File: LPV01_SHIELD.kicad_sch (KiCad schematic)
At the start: 98 parts, among them J1 Screw_Terminal_01x02, J10 SPI_header, J11 Power_socket, J12 USB1035-GF-P-0-B-B, J13 USB1035-GF-P-0-B-B, J14 USB1035-GF-P-0-B-B, J15 Screw_Terminal_01x03, J16 Screw_Terminal_01x03, J17 Wiegand, J18 A-USBSA, J19 Screw_Terminal_01x02, J2 Screw_Terminal_01x02, J20 Screw_Terminal_01x02, J21 Screw_Terminal_01x02, J22 Screw_Terminal_01x02, J23 GND, J3 Screw_Terminal_01x02, J4 Screw_Terminal_01x02, J5 Screw_Terminal_01x02, J6 Screw_Terminal_01x02, J7 Screw_Terminal_01x02, J8 Screw_Terminal_01x02, J9 GPIO_header, Q1 BC817, Q2 BC817, Q3 BC817, Q4 BC817, Q5 BC817, Q6 BC817, Q7 BC817, Q8 BC817, SW1 SW_SPST, SW2 SW_SPST, SW3 SW_SPST, SW4 SW_SPST, SW5 SW_SPST, SW6 SW_SPST, SW7 SW_SPST, SW8 SW_SPST, U1 TLP175A, U12 USB2517I-JZX, U13 FT2232HQ, U16 M24C02-FMN, U2 TLP175A, U3 TLP175A, U4 TLP175A, U5 TLP175A, U6 TLP175A, U7 TLP175A, U8 TLP175A

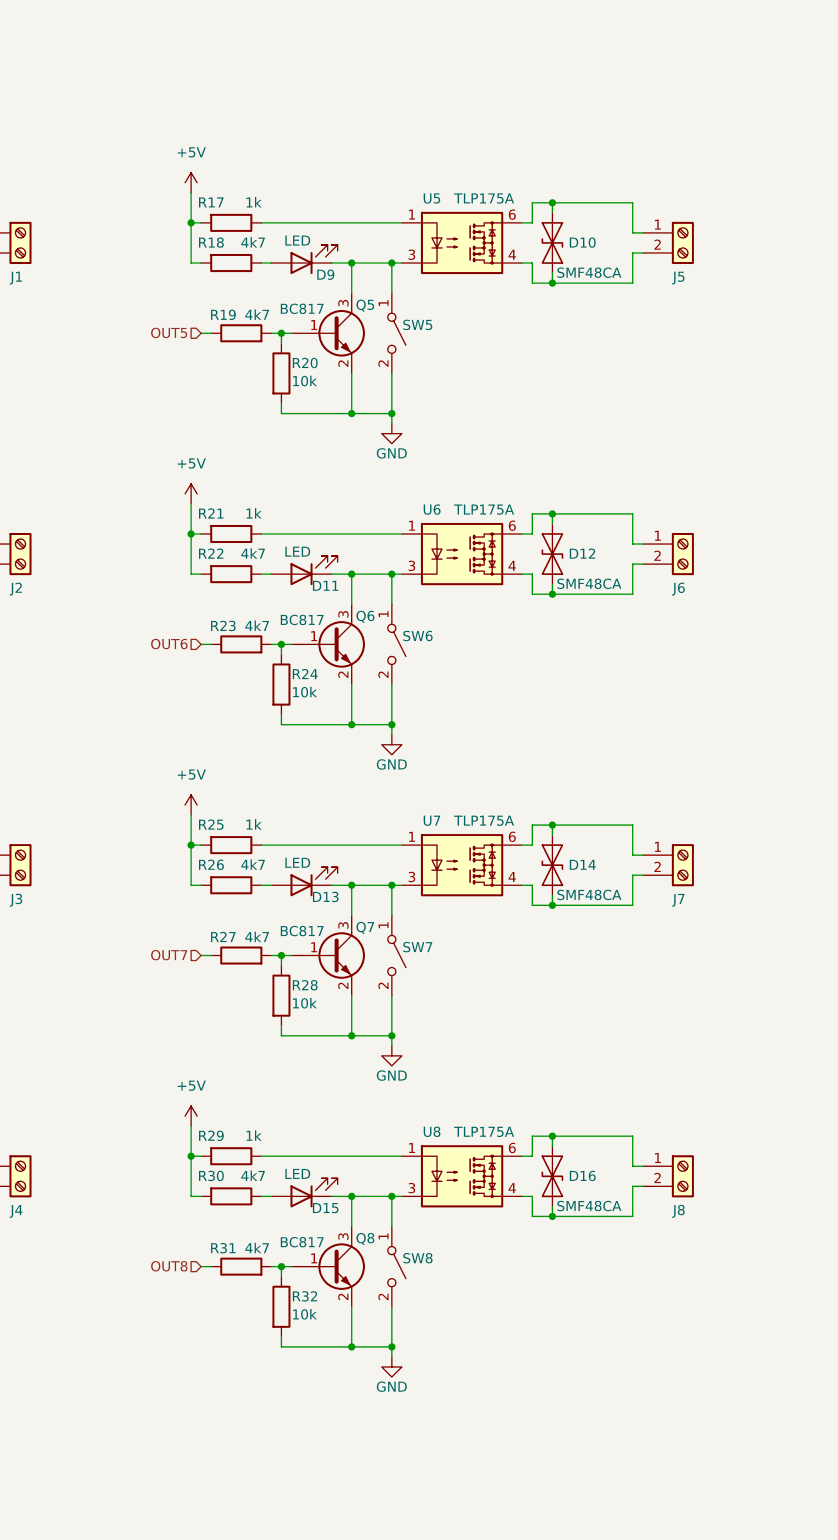
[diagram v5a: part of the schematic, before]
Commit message: Changes in schematic to fit DC/DC converter
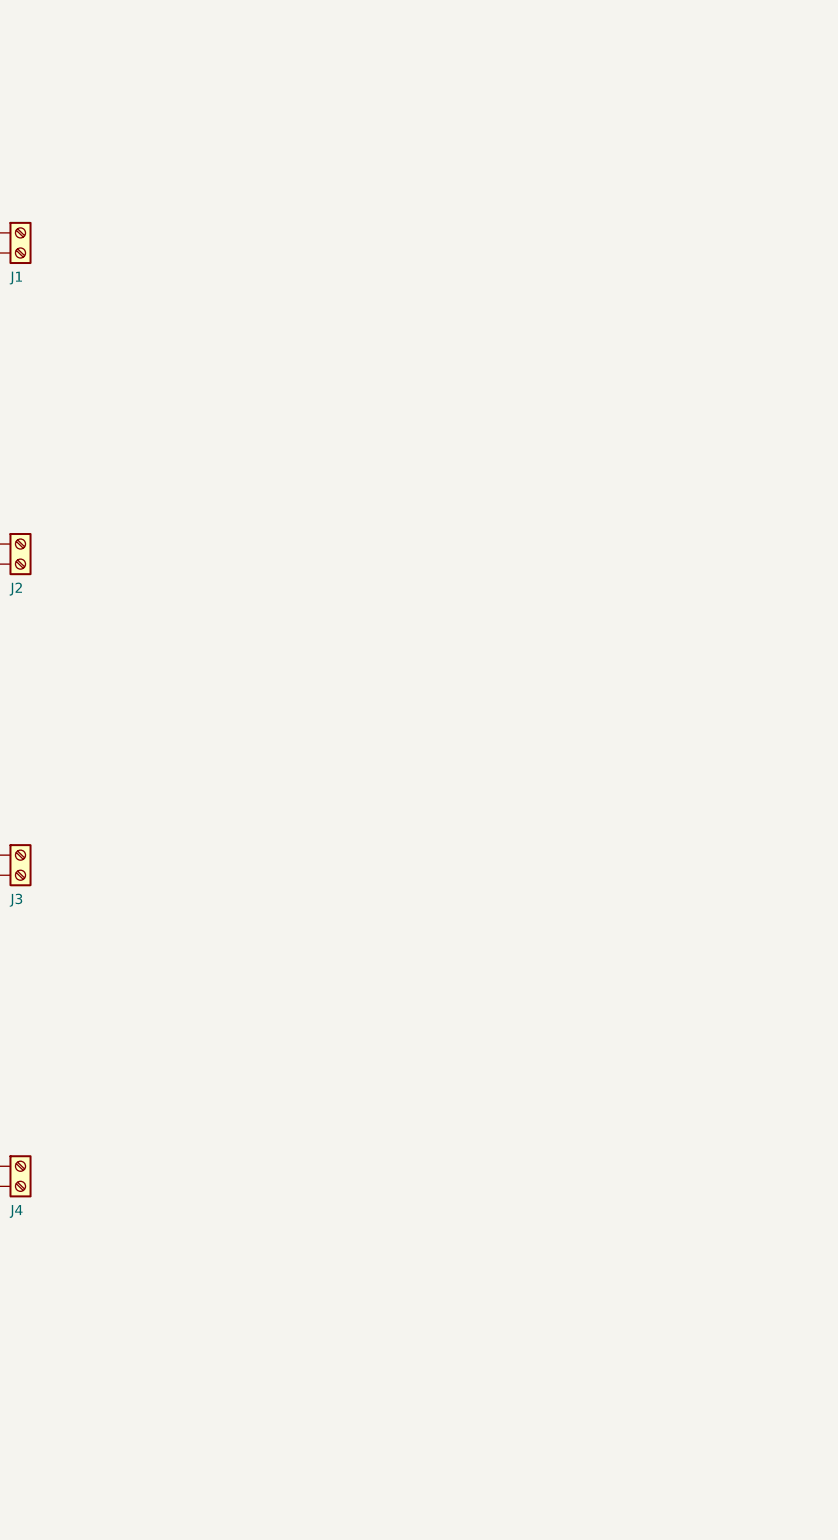
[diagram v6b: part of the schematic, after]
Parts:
- removed D10, D12, D14, D16: SMF48CA, Diode_SMD:D_SMA, symbol Diode:SD36_SOD323
- removed D11, D13, D15, D9: LED, LED_SMD:LED_0603_1608Metric, symbol Device:LED
- removed J5, J6, J7, J8: Screw_Terminal_01x02, TerminalBlock_Phoenix:TerminalBlock_Phoenix_MKDS-1,5-2_1x02_P5.00mm_Horizontal, symbol Connector:Screw_Terminal_01x02
- removed Q5, Q6, Q7, Q8: BC817, Package_TO_SOT_SMD:SOT-23, symbol Transistor_BJT:BC817
- removed R17, R21, R25, R29: 1k, Resistor_SMD:R_0603_1608Metric, symbol Device:R
- removed R18, R19, R22, R23, R26, R27, R30, R31: 4k7, Resistor_SMD:R_0603_1608Metric, symbol Device:R
- removed R20, R24, R28, R32: 10k, Resistor_SMD:R_0603_1608Metric, symbol Device:R
- removed SW5, SW6, SW7, SW8: SW_SPST, Button_Switch_SMD:SW_SPST_CK_RS282G05A3, symbol Switch:SW_SPST
- removed U5, U6, U7, U8: TLP175A, Package_SO:MFSOP6-4_4.4x3.6mm_P1.27mm, symbol Relay_SolidState:TLP175A

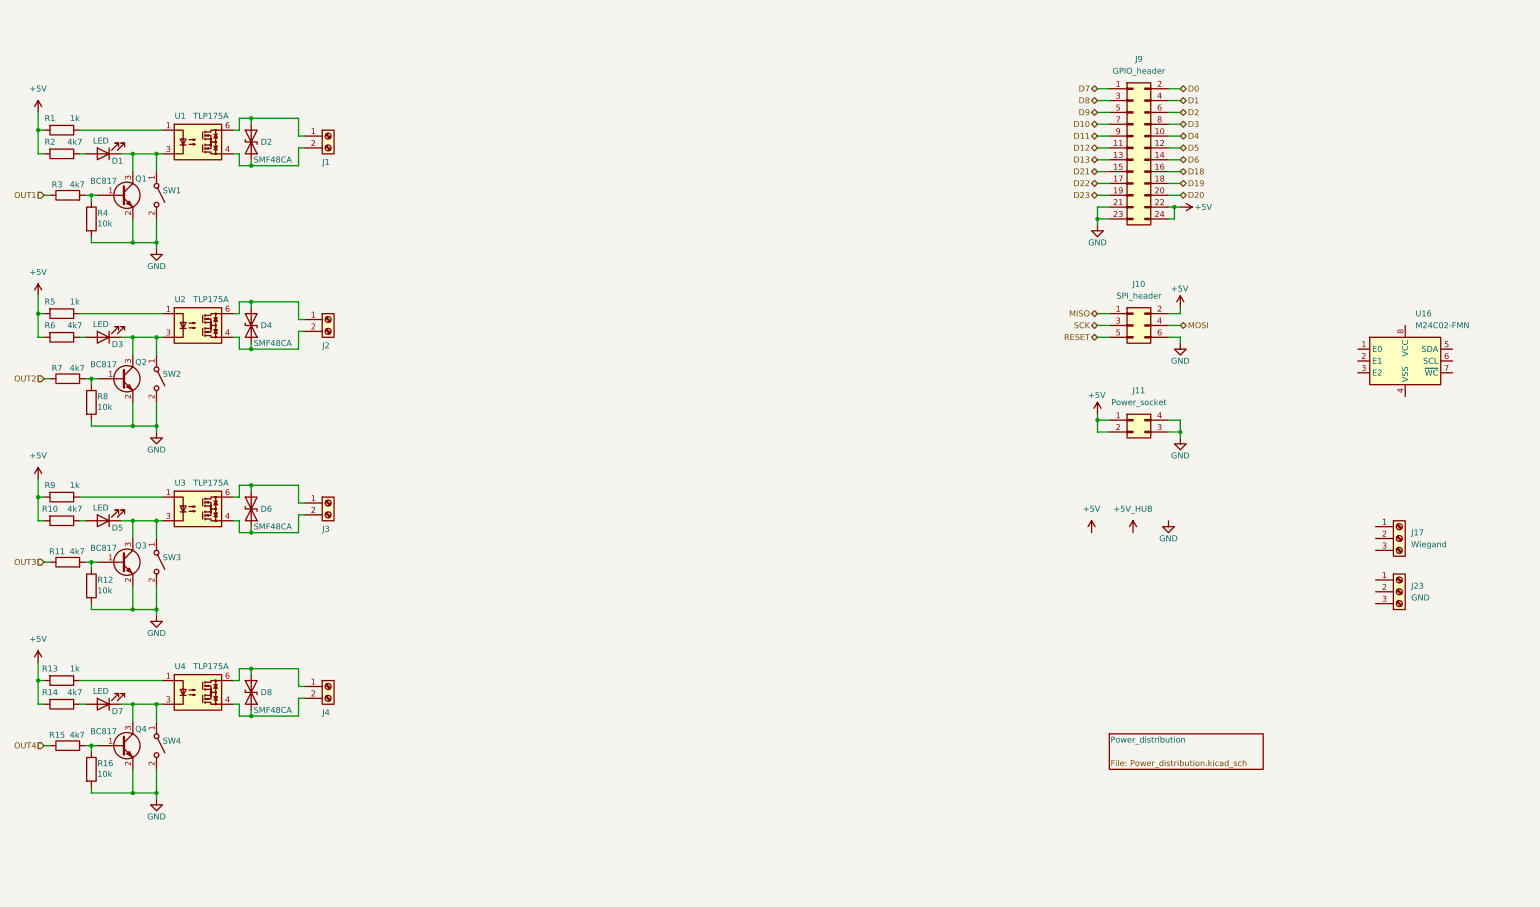
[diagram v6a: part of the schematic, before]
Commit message: Added 2 schematic sheets
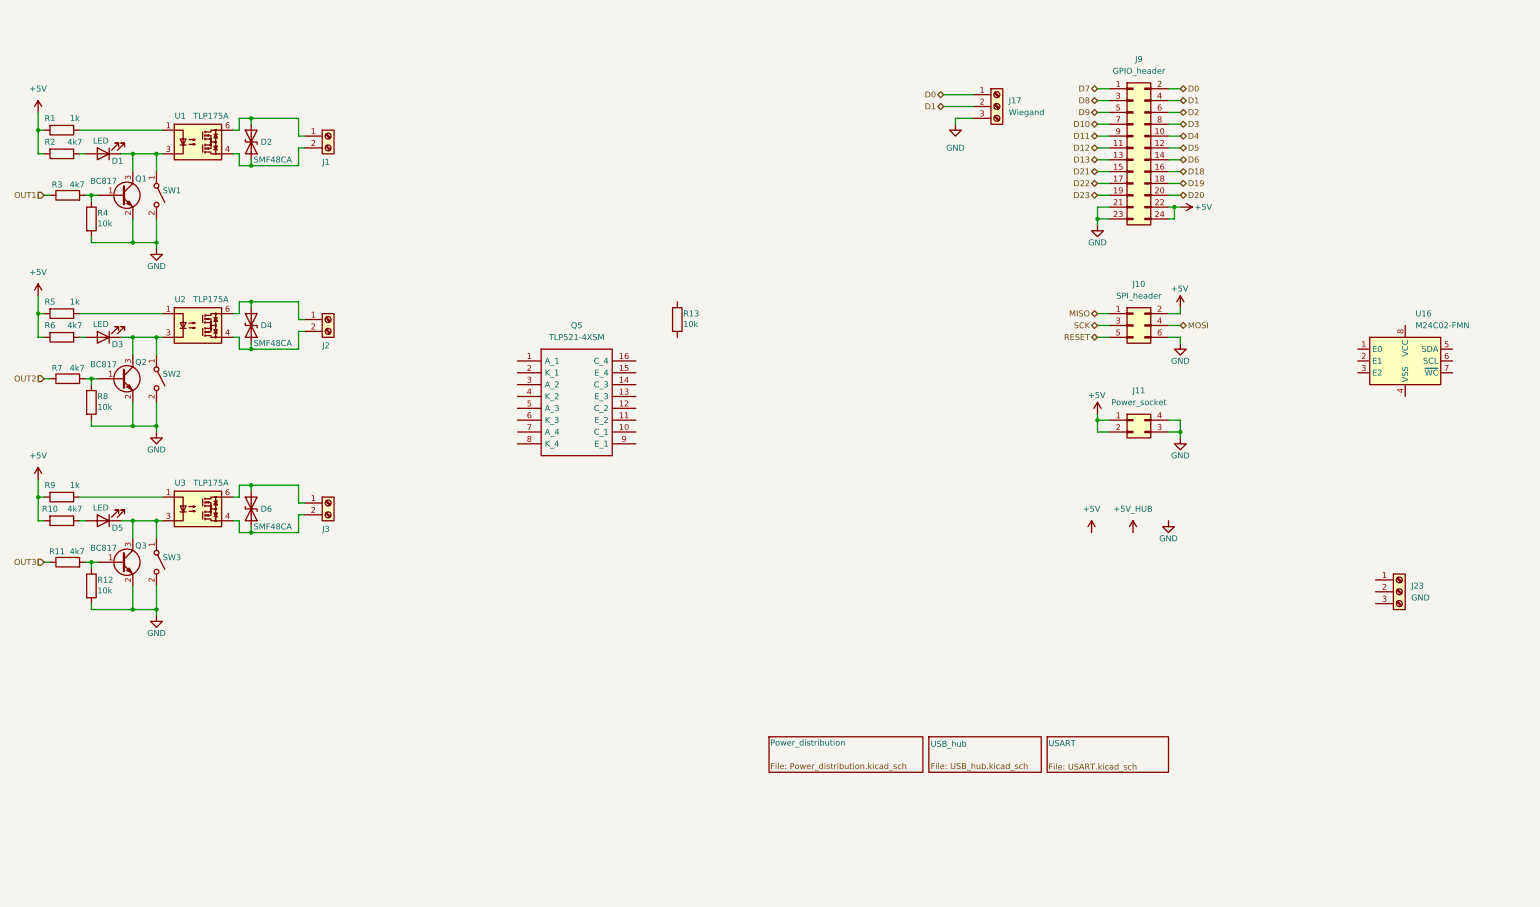
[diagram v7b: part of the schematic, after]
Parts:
- removed D7: LED, LED_SMD:LED_0603_1608Metric, symbol Device:LED
- removed D8: SMF48CA, Diode_SMD:D_SMA, symbol Diode:SD36_SOD323
- removed J4: Screw_Terminal_01x02, TerminalBlock_Phoenix:TerminalBlock_Phoenix_MKDS-1,5-2_1x02_P5.00mm_Horizontal, symbol Connector:Screw_Terminal_01x02
- removed Q4: BC817, Package_TO_SOT_SMD:SOT-23, symbol Transistor_BJT:BC817
- removed R14, R15: 4k7, Resistor_SMD:R_0603_1608Metric, symbol Device:R
- removed R16: 10k, Resistor_SMD:R_0603_1608Metric, symbol Device:R
- removed SW4: SW_SPST, Button_Switch_SMD:SW_SPST_CK_RS282G05A3, symbol Switch:SW_SPST
- removed U4: TLP175A, Package_SO:MFSOP6-4_4.4x3.6mm_P1.27mm, symbol Relay_SolidState:TLP175A
- added Q5: TLP521-4XSM, SamacSys_Parts:TLP5214XSM, symbol SamacSys_Parts:TLP521-4XSM
- J17: footprint TerminalBlock_Phoenix:TerminalBlock_Phoenix_MKDS-1,5-3_1x03_P5.00mm_Horizontal -> TerminalBlock_Phoenix:TerminalBlock_Phoenix_PT-1,5-3-3.5-H_1x03_P3.50mm_Horizontal
- J18: footprint A-USBSA -> SamacSys_Parts:A-USBSA
- R13: value 1k -> 10k
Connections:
- net +5V: no longer R13.2
- net D0: now also J17.1 (Pin_1)
- net D1: now also J17.2 (Pin_2)
- net GND: now also J17.3 (Pin_3)
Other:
- added sheet USART (USART.kicad_sch)
- added sheet USB_hub (USB_hub.kicad_sch)
- moved on the sheet: J17

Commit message: Added inputs and outputs to the schematic
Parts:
- removed J12, J13, J14: USB1035-GF-P-0-B-B, SamacSys_Parts:USB1035GFP0BB, symbol SamacSys_Parts:USB1035-GF-P-0-B-B
- removed J15, J16: Screw_Terminal_01x03, TerminalBlock_Phoenix:TerminalBlock_Phoenix_MKDS-1,5-3_1x03_P5.00mm_Horizontal, symbol Connector:Screw_Terminal_01x03
- removed J18: A-USBSA, SamacSys_Parts:A-USBSA, symbol SamacSys_Parts:A-USBSA
- removed J19, J20, J21, J22: Screw_Terminal_01x02, TerminalBlock_Phoenix:TerminalBlock_Phoenix_MKDS-1,5-2_1x02_P5.00mm_Horizontal, symbol Connector:Screw_Terminal_01x02
- removed J23: GND, TerminalBlock_Phoenix:TerminalBlock_Phoenix_MKDS-1,5-3_1x03_P5.00mm_Horizontal, symbol Connector:Screw_Terminal_01x03
- removed U12: USB2517I-JZX, Package_DFN_QFN:QFN-64-1EP_9x9mm_P0.5mm_EP5.45x5.45mm_ThermalVias, symbol SamacSys_Parts:USB2517I-JZX
- removed U13: FT2232HQ, Package_DFN_QFN:QFN-64-1EP_9x9mm_P0.5mm_EP4.35x4.35mm, symbol Interface_USB:FT2232HQ
- removed U16: M24C02-FMN, Package_SO:SOIC-8_3.9x4.9mm_P1.27mm, symbol Memory_EEPROM:M24C02-FMN
- added D10, D11, D12, D13, D14, D15, D7, D8: LED, symbol Device:LED
- added D16, D19, D21, D23, D25, D27, D30, D31: D, symbol Device:D
- added D17, D18, D20, D22, D24, D26, D28, D29: LED, LED_SMD:LED_0603_1608Metric, symbol Device:LED
- added J15, J22: Inputs, TerminalBlock_Phoenix:TerminalBlock_Phoenix_PT-1,5-8-3.5-H_1x08_P3.50mm_Horizontal, symbol Connector:Screw_Terminal_01x08
- added J16, J23: Screw_Terminal_01x02, TerminalBlock_Phoenix:TerminalBlock_Phoenix_PT-1,5-2-3.5-H_1x02_P3.50mm_Horizontal, symbol Connector:Screw_Terminal_01x02
- added J24: Conn_01x02_Pin, symbol Connector:Conn_01x02_Pin
- added Q10, Q11, Q12, Q13, Q14, Q15, Q7, Q9: BC817, Package_TO_SOT_SMD:SOT-23, symbol Transistor_BJT:BC817
- added Q4, Q6, Q8: TLP521-4XSM, SamacSys_Parts:TLP5214XSM, symbol SamacSys_Parts:TLP521-4XSM
- added R14, R29, R30, R31, R32, R33, R34, R35: 2k2, Resistor_SMD:R_0603_1608Metric, symbol Device:R
- added R15, R16, R28, R36, R38, R39, R40, R41, R42, R43, R44, R45, R46, R47: 10k, Resistor_SMD:R_0603_1608Metric, symbol Device:R
- added R37: 10k ->, Resistor_SMD:R_0603_1608Metric, symbol Device:R
- added R48, R49, R50, R51, R52, R53, R54, R55, R56, R57, R58, R59, R60, R61, R62, R63: 1k, Resistor_SMD:R_0603_1608Metric, symbol Device:R
- added SW10, SW11, SW4, SW5, SW6, SW7, SW8, SW9: SW_SPST, Button_Switch_SMD:SW_SPST_CK_RS282G05A3, symbol Switch:SW_SPST
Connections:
- net +5V: now also R13.1, Q6.10 (C_1), Q6.12 (C_2), Q6.14 (C_3), Q6.16 (C_4), Q8.10 (C_1), Q8.12 (C_2), Q8.14 (C_3), Q8.16 (C_4), R15.1, R16.1, R28.1, R44.1, R45.1, R46.1, R47.1, SW10.1 (A), SW11.1 (A), SW4.1 (A), SW5.1 (A), SW6.1 (A), SW7.1 (A), SW8.1 (A), SW9.1 (A)
- net D10: now also R49.2
- net D11: now also R50.2
- net D12: now also R51.2
- net D18: now also R53.2
- net D19: now also R54.2
- net D2: now also Q5.16 (C_4), R13.2
- net D21: now also R52.2
- net D22: now also R55.2
- net D23: now also R56.2
- net D3: now also Q5.14 (C_3), R15.2
- net D4: now also Q5.12 (C_2), R16.2
- net D5: now also Q5.10 (C_1), R28.2
- net D6: now also Q4.16 (C_4), R44.2
- net D7: now also Q4.14 (C_3), R45.2
- net D8: now also Q4.12 (C_2), R46.2
- net D9: now also Q4.10 (C_1), R47.2
- net GND: now also Q5.11 (E_2), Q5.13 (E_3), Q5.15 (E_4), Q5.9 (E_1), J16.1 (Pin_1), J16.2 (Pin_2), J23.2 (Pin_2), Q10.2 (E), Q11.2 (E), Q12.2 (E), Q13.2 (E), Q14.2 (E), Q15.2 (E), Q4.11 (E_2), Q4.13 (E_3), Q4.15 (E_4), Q4.9 (E_1), Q6.2 (K_1), Q6.4 (K_2), Q6.6 (K_3), Q6.8 (K_4), Q7.2 (E), Q8.2 (K_1), Q8.4 (K_2), Q8.6 (K_3), Q8.8 (K_4), Q9.2 (E)
- net MISO: now also R3.1
- net MOSI: now also R11.1
- net OUT1: now also D16.2 (A), J22.1 (Pin_1), Q7.3 (C); no longer R3.1
- net OUT2: now also D19.2 (A), J22.2 (Pin_2), Q9.3 (C); no longer R7.1
- net OUT3: now also D21.2 (A), J22.3 (Pin_3), Q10.3 (C); no longer R11.1
- net SCK: now also R7.1
- net at Q5.1 (A_1): now also D7.1 (K)
- net at Q5.2 (K_1): now also J15.8 (Pin_8), R37.2
- net at Q5.3 (A_2): now also D10.1 (K)
- net at Q5.4 (K_2): now also J15.7 (Pin_7), R36.2
- net at Q5.5 (A_3): now also D11.1 (K)
- net at Q5.6 (K_3): now also J15.6 (Pin_6), R38.2
- net at Q5.7 (A_4): now also D8.1 (K)
- net at Q5.8 (K_4): now also J15.5 (Pin_5), R39.2
- new net: Q12.1 (B), R60.2
- new net: D29.1 (K), R63.1
- new net: Q10.1 (B), R58.2
- new net: Q7.1 (B), R48.2
- new net: D12.1 (K), Q4.1 (A_1)
- new net: D12.2 (A), R32.1
- new net: D10.2 (A), R29.1
- new net: J15.4 (Pin_4), Q4.2 (K_1), R40.2
- new net: D13.1 (K), Q4.3 (A_2)
- new net: J15.3 (Pin_3), Q4.4 (K_2), R41.2
- new net: D14.1 (K), Q4.5 (A_3)
- new net: J15.2 (Pin_2), Q4.6 (K_3), R42.2
- new net: D15.1 (K), Q4.7 (A_4)
- new net: J15.1 (Pin_1), Q4.8 (K_4), R43.2
- new net: D15.2 (A), R35.1
- new net: D17.1 (K), R48.1
- new net: D11.2 (A), R30.1
- new net: Q8.5 (A_3), R55.1
- new net: Q8.1 (A_1), R53.1
- new net: Q8.3 (A_2), R54.1
- new net: Q8.7 (A_4), R56.1
- new net: D22.1 (K), R59.1
- new net: Q11.1 (B), R59.2
- new net: Q14.1 (B), R62.2
- new net: D13.2 (A), R33.1
- new net: D18.1 (K), R57.1
- new net: D20.1 (K), R58.1
- new net: D7.2 (A), R14.1
- new net: D14.2 (A), R34.1
- new net: Q13.1 (B), R61.2
- new net: D8.2 (A), R31.1
- new net: Q6.1 (A_1), R49.1
- new net: Q6.3 (A_2), R50.1
- new net: Q6.5 (A_3), R51.1
- new net: Q6.7 (A_4), R52.1
- new net: Q9.1 (B), R57.2
- new net: D26.1 (K), R61.1
- new net: Q15.1 (B), R63.2
- new net: D24.1 (K), R60.1
- new net: D28.1 (K), R62.1
- new net +24V: J24.1 (Pin_1), R14.2, R29.2, R30.2, R31.2, R32.2, R33.2, R34.2, R35.2, R36.1, R37.1, R38.1, R39.1, R40.1, R41.1, R42.1, R43.1
- new net O1: D17.2 (A), D18.2 (A), D20.2 (A), D22.2 (A), D24.2 (A), D26.2 (A), D28.2 (A), D29.2 (A), Q6.15 (E_4), SW10.2 (B), SW11.2 (B), SW4.2 (B), SW5.2 (B), SW6.2 (B), SW7.2 (B), SW8.2 (B), SW9.2 (B)
- new net O2: Q6.13 (E_3)
- new net O3: Q6.11 (E_2)
- new net O4: Q6.9 (E_1)
- new net O5: Q8.15 (E_4)
- new net O6: Q8.13 (E_3)
- new net O7: Q8.11 (E_2)
- new net O8: Q8.9 (E_1)
- new net OUT4: D23.2 (A), J22.4 (Pin_4), Q11.3 (C)
- new net OUT5: D27.2 (A), J22.5 (Pin_5), Q13.3 (C)
- new net OUT6: D25.2 (A), J22.6 (Pin_6), Q12.3 (C)
- new net OUT7: D30.2 (A), J22.7 (Pin_7), Q14.3 (C)
- new net OUT8: D31.2 (A), J22.8 (Pin_8), Q15.3 (C)
- new net VR: D16.1 (K), D19.1 (K), D21.1 (K), D23.1 (K), D25.1 (K), D27.1 (K), D30.1 (K), D31.1 (K), J23.1 (Pin_1), J24.2 (Pin_2)
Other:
- moved on the sheet: D1, D2, D3, D4, D5, D6, J1, J10, J11, J17, J2, J3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
